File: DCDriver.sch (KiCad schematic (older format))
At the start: 3 parts, among them U4 IFX9201

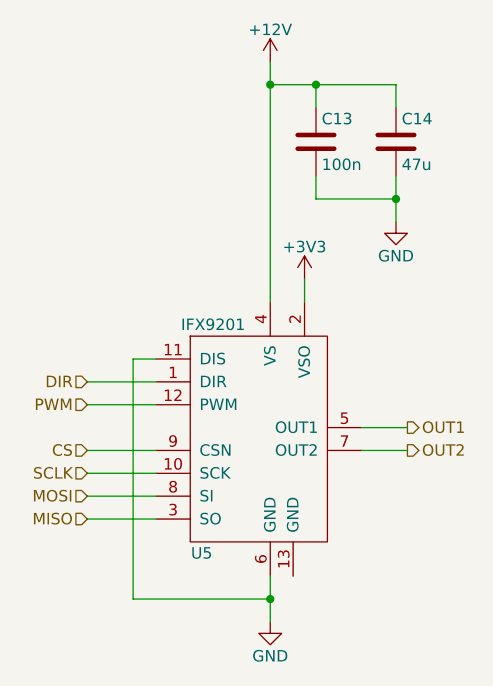
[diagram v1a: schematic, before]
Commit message: Finalized BOM and reworked AUX pins.
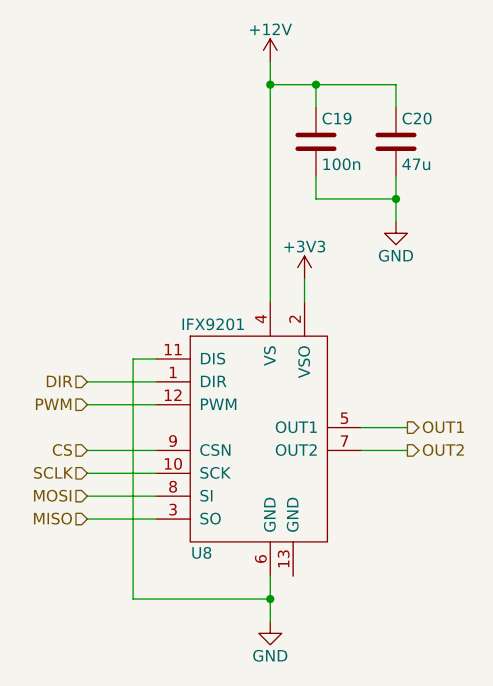
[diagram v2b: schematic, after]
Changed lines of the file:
@@
 AR Path="/5FC48379/5F9F9AE9" Ref="U7"  Part="1"
 AR Path="/5FC79084/5F9F9AE9" Ref="U8"  Part="1"
-F 0 "U5" H 4450 4350 50  0000 C CNN
+F 0 "U8" H 4450 4350 50  0000 C CNN
 F 1 "IFX9201" H 4500 5350 50  0000 C CNN
 F 2 "Package_SO:Infineon_PG-DSO-12-9_ThermalVias" H 4350 4650 50  0001 C CNN
@@
 AR Path="/5FC48379/5F9FAF7F" Ref="#PWR038"  Part="1"
 AR Path="/5FC79084/5F9FAF7F" Ref="#PWR042"  Part="1"
-F 0 "#PWR030" H 4900 3100 50  0001 C CNN
+F 0 "#PWR042" H 4900 3100 50  0001 C CNN
 F 1 "+3V3" H 4900 3390 50  0000 C CNN
 F 2 "" H 4900 3250 50  0001 C CNN
@@
 AR Path="/5FC48379/5F9FBA4F" Ref="#PWR039"  Part="1"
 AR Path="/5FC79084/5F9FBA4F" Ref="#PWR043"  Part="1"
-F 0 "#PWR031" H 4750 4500 50  0001 C CNN
+F 0 "#PWR043" H 4750 4500 50  0001 C CNN
 F 1 "GND" H 4750 4600 50  0000 C CNN
 F 2 "" H 4750 4750 50  0001 C CNN
@@
 AR Path="/5FC48379/5F92A42F" Ref="#PWR036"  Part="1"
 AR Path="/5FC79084/5F92A42F" Ref="#PWR040"  Part="1"
-F 0 "#PWR028" H 4750 2150 50  0001 C CNN
+F 0 "#PWR040" H 4750 2150 50  0001 C CNN
 F 1 "+12V" H 4750 2440 50  0000 C CNN
 F 2 "" H 4750 2300 50  0001 C CNN
@@
 AR Path="/5FC48379/5F9FF9F3" Ref="C17"  Part="1"
 AR Path="/5FC79084/5F9FF9F3" Ref="C19"  Part="1"
-F 0 "C13" H 4975 2750 50  0000 L CNN
+F 0 "C19" H 4975 2750 50  0000 L CNN
 F 1 "100n" H 4975 2550 50  0000 L CNN
 F 2 "Capacitor_SMD:C_0805_2012Metric" H 4988 2500 50  0001 C CNN
@@
 AR Path="/5FC48379/5F9FF9FC" Ref="C18"  Part="1"
 AR Path="/5FC79084/5F9FF9FC" Ref="C20"  Part="1"
-F 0 "C14" H 5325 2750 50  0000 L CNN
+F 0 "C20" H 5325 2750 50  0000 L CNN
 F 1 "47u" H 5325 2550 50  0000 L CNN
 F 2 "Capacitor_SMD:CP_Elec_6.3x5.9" H 5338 2500 50  0001 C CNN
@@
 AR Path="/5FC48379/5FA01470" Ref="#PWR037"  Part="1"
 AR Path="/5FC79084/5FA01470" Ref="#PWR041"  Part="1"
-F 0 "#PWR029" H 5300 2750 50  0001 C CNN
+F 0 "#PWR041" H 5300 2750 50  0001 C CNN
 F 1 "GND" H 5300 2850 50  0000 C CNN
 F 2 "" H 5300 3000 50  0001 C CNN

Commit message: Revision v0.1 of PCB fully complete.
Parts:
- C11: LCSC (none) -> C49678; SKU 302010165 -> (none)
- U4: LCSC (none) -> C112633
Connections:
- net GND: now also U4.13 (GND)
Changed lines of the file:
@@
 F 5 "IFX9201SGAUMA1 " H 4400 4400 50  0001 C CNN "MPN"
 F 6 "3.55" H 4400 4400 50  0001 C CNN "Price"
+F 7 "C112633" H 4400 4400 50  0001 C CNN "LCSC"
 	1    4400 4400
 	1    0    0    -1
@@
 F 5 "Yageo" H 4950 2650 50  0001 C CNN "MFR"
 F 6 "0.046" H 4950 2650 50  0001 C CNN "Price"
-F 7 "302010165" H 4950 2650 50  0001 C CNN "SKU"
+F 7 "" H 4950 2650 50  0001 C CNN "SKU"
+F 8 "C49678" H 4950 2650 50  0001 C CNN "LCSC"
 	1    4950 2650
 	1    0    0    -1
@@
 Wire Wire Line
 	3950 4300 4250 4300
+Wire Wire Line
+	4750 4650 4850 4650
+Wire Wire Line
+	4850 4650 4850 4550
 $EndSCHEMATC
